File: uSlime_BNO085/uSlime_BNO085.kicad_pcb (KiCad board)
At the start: 2 copper layers, 16.7 x 12.8 mm, 15 parts, among them CN1 X1502WR-05K-N0SN, U5 BNO085

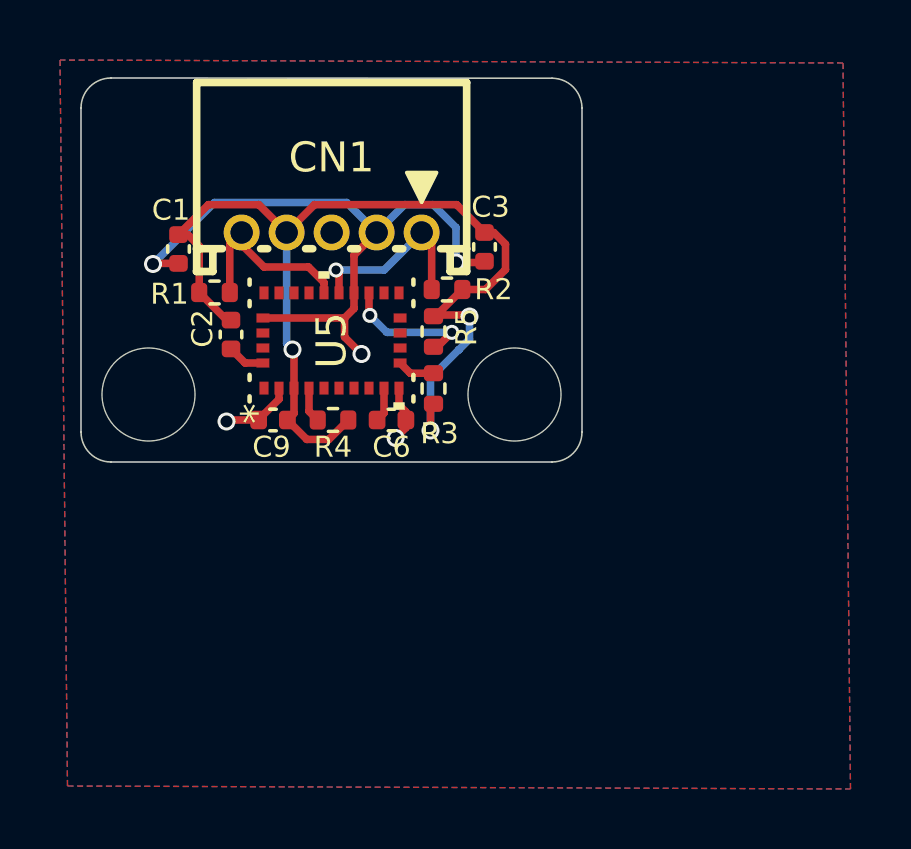
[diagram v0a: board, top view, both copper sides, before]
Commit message: Faulty BNO085 footprint
First, I do not like you UltraLibrarian anymore, for you have wasted a
lot of time and effort (and money) on footprints that are just straight
up wrong. I am this close to unleashing unbridled rage on this but will
bottle it up for now.

Second, I took the BNO085 footprint from the official SlimeVR tracker
and put it in this project. At least they have the right footprint...

Stencils for the main microcontroller does not need to change but the
extension module got a revamp in favor of being more versatile. You can
now choose which I2C address the sensor operates on; just make sure you
bridge the right contacts.
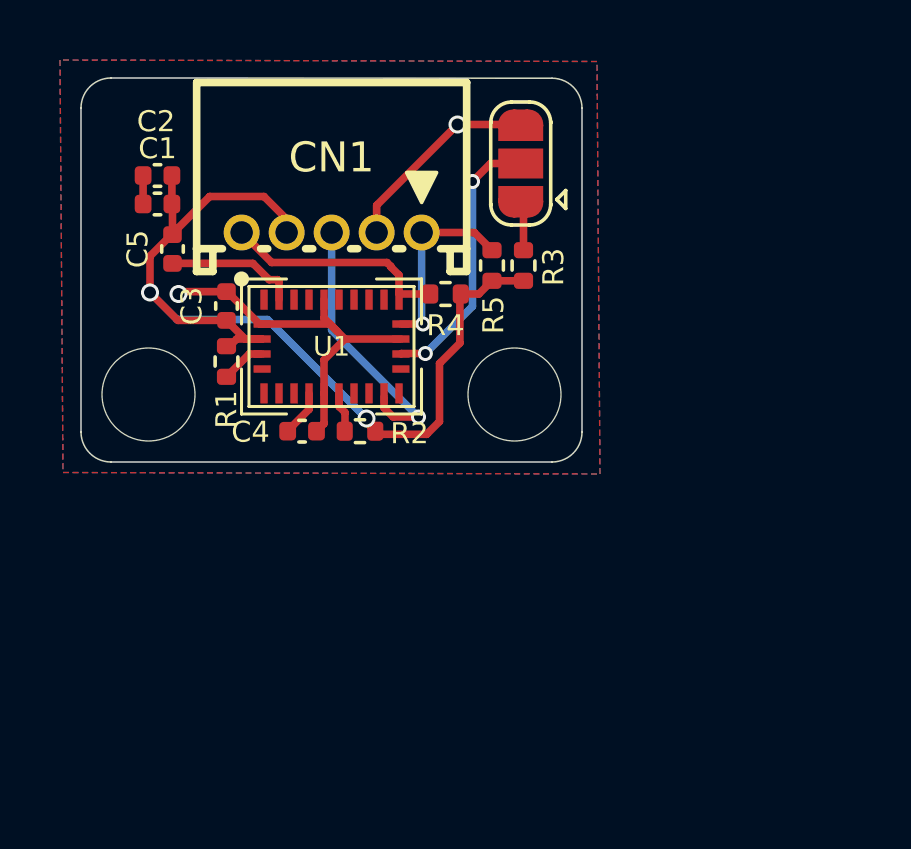
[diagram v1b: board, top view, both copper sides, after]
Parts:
- removed C6, C9: 0.1uF, Capacitor_SMD:C_0402_1005Metric
- added C4: 0.1uF, Capacitor_SMD:C_0402_1005Metric, F.Cu at (108.0, 101.1)
- added C5: 0.1uF, Capacitor_SMD:C_0402_1005Metric, F.Cu at (103.7, 95.0)
- added JP1: Jumper_3_Open, Jumper:SolderJumper-3_P1.3mm_Open_RoundedPad1.0x1.5mm, F.Cu at (115.3, 92.2)
- R1, R2: value 2.2k -> 10k
- R4, R5: value 10k -> 2.2k
- U1: renamed from U5; footprint uSlime-libs:LGA28_5.2X3.8_CEV -> uSlime-libs:BNO080
- moved C3 8.82 mm to (105.5, 97.0)
- moved C2 5.84 mm to (103.2, 92.6), turned to 0 degrees
- moved R4 5.63 mm to (112.8, 96.5), turned to 0 degrees
- moved R2 5.54 mm to (110.0, 101.1), turned to 180 degrees
- moved R3 5.08 mm to (115.4, 95.6)
- moved R5 2.94 mm to (114.3, 95.6)
- moved R1 2.33 mm to (105.5, 98.8), turned to -90 degrees
- moved C1 1.66 mm to (103.2, 93.5), turned to 0 degrees
- moved U1 0.20 mm to (109.0, 98.3), turned to 0 degrees
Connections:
- C2 pad 1: Net-(U5-VDDIO) -> GND
- C3 pad 1: GND -> +3.3V
- C3 pad 2: +3.3V -> GND
- R1 pad 1: BNO_SDA -> +3.3V
- R1 pad 2: +3.3V -> Net-(U1-BOOTN)
- R2 pad 1: BNO_SCL -> +3.3V
- R2 pad 2: +3.3V -> Net-(U1-NRST)
- R3 pad 2: Net-(U5-NRST) -> Net-(JP1-A)
- R4 pad 1: +3.3V -> BNO_SDA
- R4 pad 2: Net-(U5-BOOTN) -> +3.3V
- R5 pad 1: +3.3V -> BNO_SCL
- R5 pad 2: Net-(U5-SA0/H_MOSI) -> +3.3V
- U1 pad 11: Net-(U5-NRST) -> Net-(U1-NRST)
- U1 pad 14: BNO_INT -> BNO_INT2
- U1 pad 17: Net-(U5-SA0/H_MOSI) -> Net-(JP1-C)
- U1 pad 28: Net-(U5-VDDIO) -> Net-(U1-VDDIO)
- U1 pad 4: Net-(U5-BOOTN) -> Net-(U1-BOOTN)
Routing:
- net Net-(JP1-C): track 0.00 -> 9.06 mm, vias 0 -> 2
- net BNO_INT2: track 0.00 -> 8.98 mm, vias 0 -> 1
- net GND: track 26.9 -> 20.6 mm, vias 5 -> 2
- net Net-(U5-SA0/H_MOSI): track 4.54 -> 0.00 mm, vias 2 -> 0
- net Net-(U1-VDDIO): track 0.00 -> 4.41 mm
- net +3.3V: track 35.9 -> 33.7 mm, vias 3 -> 2
- net Net-(JP1-A): track 0.00 -> 1.63 mm
- net Net-(U1-BOOTN): track 0.00 -> 1.50 mm
- net Net-(U1-NRST): track 0.00 -> 1.35 mm
- net BNO_SDA: track 6.18 -> 7.51 mm
- net Net-(U5-VDDIO): track 1.26 -> 0.00 mm
- net Net-(U5-NRST): track 1.25 -> 0.00 mm
- net Net-(U5-BOOTN): track 1.18 -> 0.00 mm
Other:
- board text added: "0x4A"
- board text added: "0x4B"

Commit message: Add version number v0.0.1a
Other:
- board text added: "v0.0.1a"
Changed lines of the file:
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@@
 		(tags "capacitor")
 		(property "Reference" "C3"
-			(at 0 -1.16 270)
+			(at 0 -1.16 -90)
 			(layer "F.SilkS")
 			(effects
@@
 		)
 		(property "Value" "0.1uF"
-			(at 0 1.16 270)
+			(at 0 1.16 -90)
 			(layer "F.Fab")
 			(effects
@@
 		)
 		(fp_text user "${REFERENCE}"
-			(at 0 0 270)
+			(at 0 0 -90)
 			(layer "F.Fab")
 			(effects
@@
 		(tags "capacitor")
 		(property "Reference" "C5"
-			(at 0 -1.16 270)
+			(at 0 -1.16 -90)
 			(layer "F.SilkS")
 			(effects
@@
 		)
 		(property "Value" "0.1uF"
-			(at 0 1.16 270)
+			(at 0 1.16 -90)
 			(layer "F.Fab")
 			(effects
@@
 		)
 		(fp_text user "${REFERENCE}"
-			(at 0 0 270)
+			(at 0 0 -90)
 			(layer "F.Fab")
 			(effects
@@
 		(tags "solder jumper open")
 		(property "Reference" "JP1"
-			(at 0 -1.8 270)
+			(at 0 -1.8 -90)
 			(layer "F.SilkS")
 			(hide yes)
@@
 		)
 		(property "Value" "Jumper_3_Open"
-			(at 0 1.9 270)
+			(at 0 1.9 -90)
 			(layer "F.Fab")
 			(effects
@@
 		(tags "resistor")
 		(property "Reference" "R3"
-			(at -0.05 1 270)
+			(at -0.05 1 -90)
 			(layer "F.SilkS")
 			(effects
@@
 		)
 		(property "Value" "10k"
-			(at 0 1.17 270)
+			(at 0 1.17 -90)
 			(layer "F.Fab")
 			(effects
@@
 		)
 		(fp_text user "${REFERENCE}"
-			(at 0 0 270)
+			(at 0 0 -90)
 			(layer "F.Fab")
 			(effects
@@
 		)
 	)
+	(gr_text "v0.0.1a"
+		(at 103.15 93 -90)
+		(layer "B.SilkS")
+		(effects
+			(font
+				(size 0.7 0.7)
+				(thickness 0.1)
+			)
+			(justify mirror)
+		)
+	)

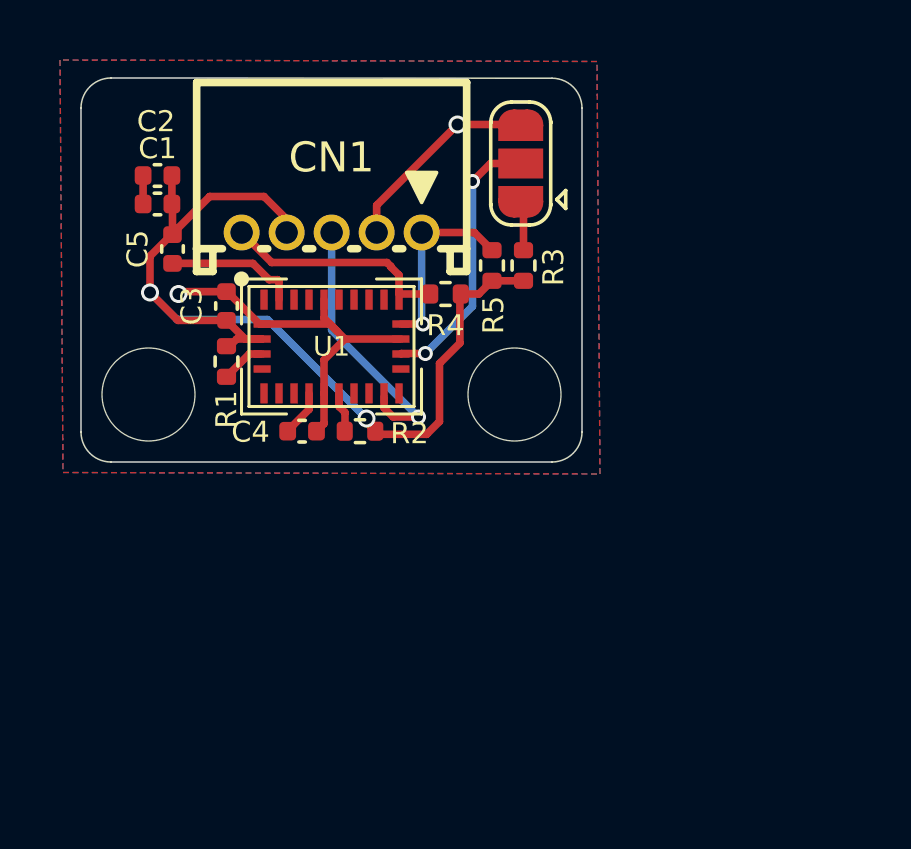
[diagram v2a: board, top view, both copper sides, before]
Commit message: v0.0.2a Modify BNO I2C
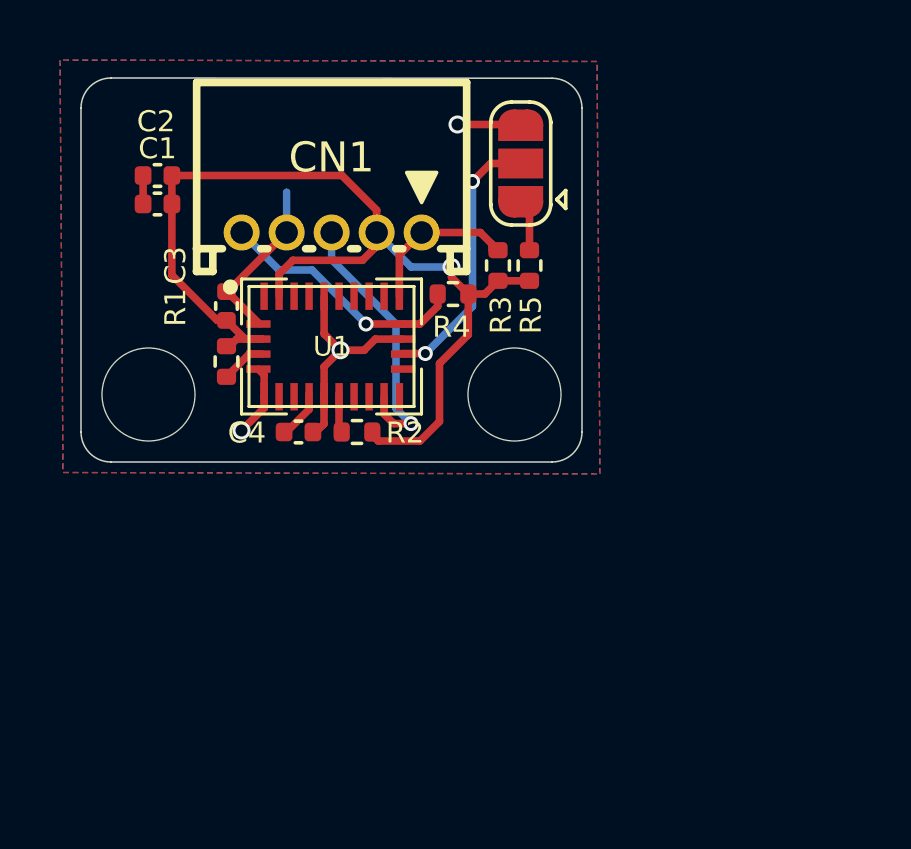
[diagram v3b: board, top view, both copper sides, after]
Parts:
- removed C5: 0.1uF, Capacitor_SMD:C_0402_1005Metric
- R3: value 10k -> 2.2k
- R5: value 2.2k -> 10k
- moved R5 1.25 mm to (115.6, 95.6)
- moved R3 0.85 mm to (114.5, 95.6)
- moved R4 0.25 mm to (113.0, 96.5), turned to 180 degrees
- moved C4 0.12 mm to (107.9, 101.2)
- moved R2 0.10 mm to (109.8, 101.2), turned to 0 degrees
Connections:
- CN1 pad 1: BNO_SCL -> BNO_SDA
- CN1 pad 2: GND -> +3.3V
- CN1 pad 4: +3.3V -> GND
- CN1 pad 5: BNO_SDA -> BNO_SCL
- R2 pad 1: +3.3V -> Net-(U1-NRST)
- R2 pad 2: Net-(U1-NRST) -> +3.3V
- R3 pad 2: Net-(JP1-A) -> BNO_SDA
- R4 pad 1: BNO_SDA -> +3.3V
- R4 pad 2: +3.3V -> BNO_SCL
- R5 pad 1: BNO_SCL -> Net-(JP1-A)
- U1 pad 28: Net-(U1-VDDIO) -> +3.3V
- U1 pad 5: unconnected-(U1-PS1-Pad5) -> GND
- U1 pad 6: unconnected-(U1-PS0/WAKE-Pad6) -> GND
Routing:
- net Net-(U1-VDDIO): track 4.41 -> 0.00 mm
- net BNO_SDA: track 7.51 -> 4.68 mm
- net BNO_SCL: track 6.39 -> 8.45 mm
- net GND: track 20.6 -> 18.8 mm, vias 2 -> 3
- net +3.3V: track 33.7 -> 34.3 mm, vias 2 -> 1
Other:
- board text added: "v0.0.2a"
- board text removed: "v0.0.1a"

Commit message: Fix BNO wrong pin order
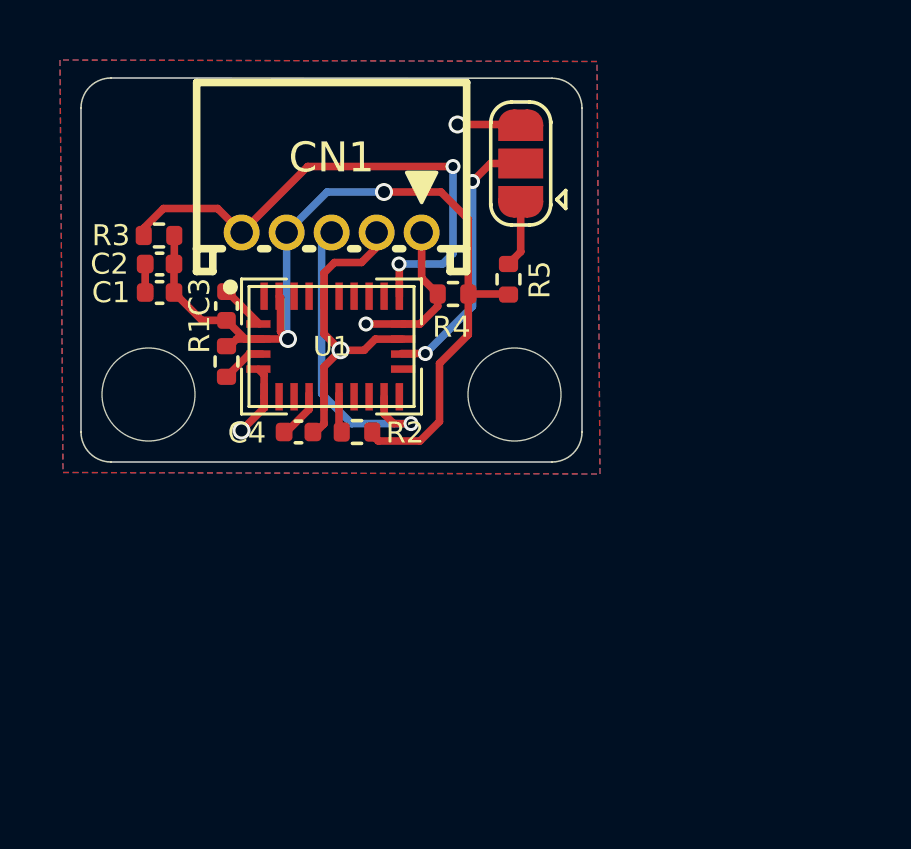
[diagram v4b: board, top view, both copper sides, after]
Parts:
- moved R3 11.3 mm to (103.2, 94.6), turned to 180 degrees
- moved C1 2.95 mm to (103.3, 96.5)
- moved C2 2.95 mm to (103.3, 95.5)
- moved R5 0.84 mm to (114.9, 96.1)
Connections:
- CN1 pad 1: BNO_SDA -> BNO_SCL
- CN1 pad 2: +3.3V -> GND
- CN1 pad 4: GND -> +3.3V
- CN1 pad 5: BNO_SCL -> BNO_SDA
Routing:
- net BNO_SDA: track 4.68 -> 18.0 mm, vias 0 -> 2
- net +3.3V: track 34.3 -> 31.0 mm, vias 1 -> 2
- net BNO_SCL: track 8.45 -> 5.32 mm
- net BNO_INT2: track 9.07 -> 10.5 mm
- net GND: track 18.8 -> 18.0 mm
- net Net-(JP1-A): track 1.51 -> 2.22 mm
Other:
- board text added: "v0.0.3a"
- board text removed: "v0.0.2a"

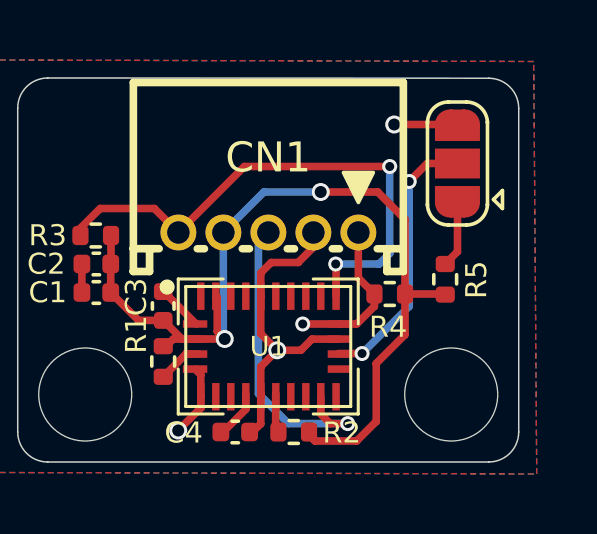
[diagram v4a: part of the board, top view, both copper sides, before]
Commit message: Connect DI without resistor
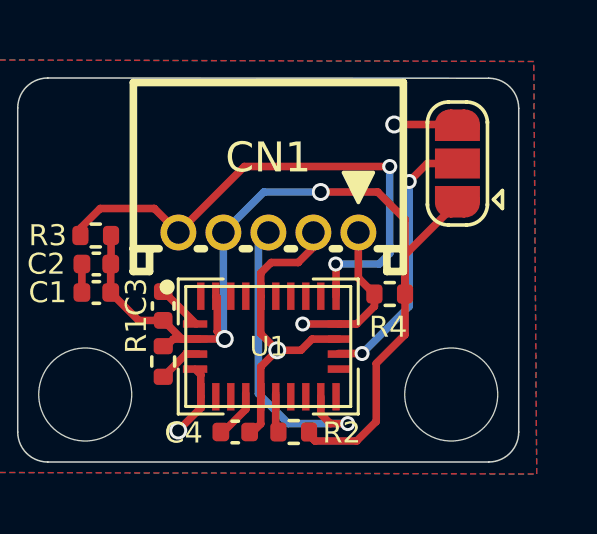
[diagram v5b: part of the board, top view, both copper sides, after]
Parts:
- removed R5: 10k, Resistor_SMD:R_0402_1005Metric
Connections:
- JP1 pad 1: Net-(JP1-A) -> +3.3V
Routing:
- net +3.3V: track 31.0 -> 33.4 mm
- net Net-(JP1-A): track 2.22 -> 0.00 mm

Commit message: v0.0.4a
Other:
- board text added: "v0.0.4a"
- board text removed: "v0.0.3a"
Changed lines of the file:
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@@
 		)
 	)
-	(gr_text "v0.0.3a"
+	(gr_text "v0.0.4a"
 		(at 103.15 93 270)
 		(layer "B.SilkS")

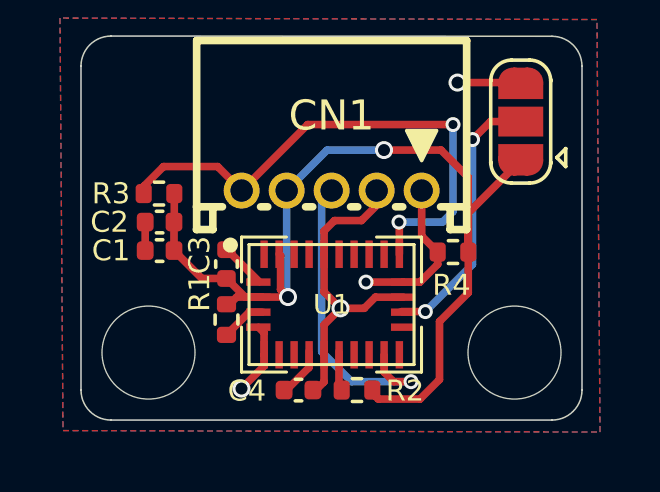
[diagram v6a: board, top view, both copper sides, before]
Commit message: v0.0.5: Invert CLKSEL pin to 3.3V
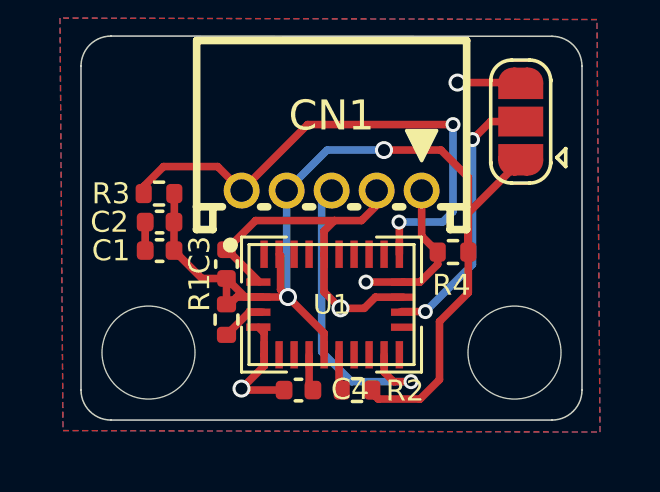
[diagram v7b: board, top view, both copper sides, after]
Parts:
- turned C4 to 0 degrees
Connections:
- U1 pad 10: GND -> +3.3V
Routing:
- net +3.3V: track 33.4 -> 36.7 mm
- net GND: track 18.0 -> 20.2 mm
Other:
- board text added: "v0.0.5a"
- board text removed: "v0.0.4a"
